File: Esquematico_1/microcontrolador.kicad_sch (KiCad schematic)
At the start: 33 parts, among them U2 STM32F405RGTx

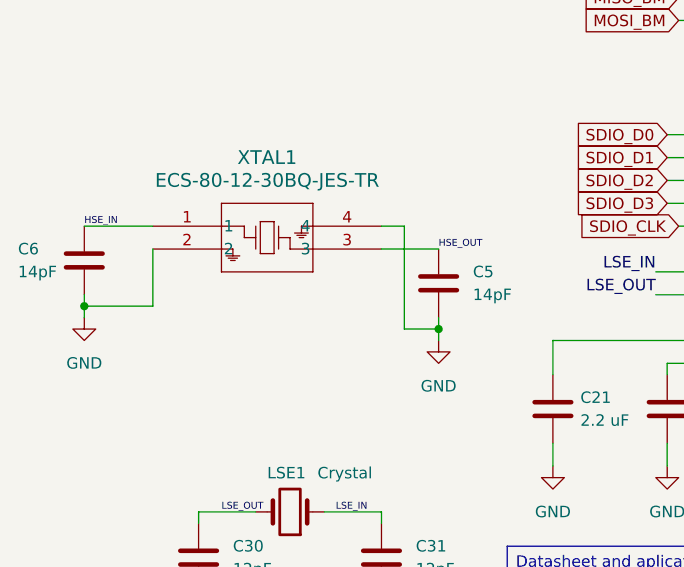
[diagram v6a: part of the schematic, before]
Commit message: asignación de footprints
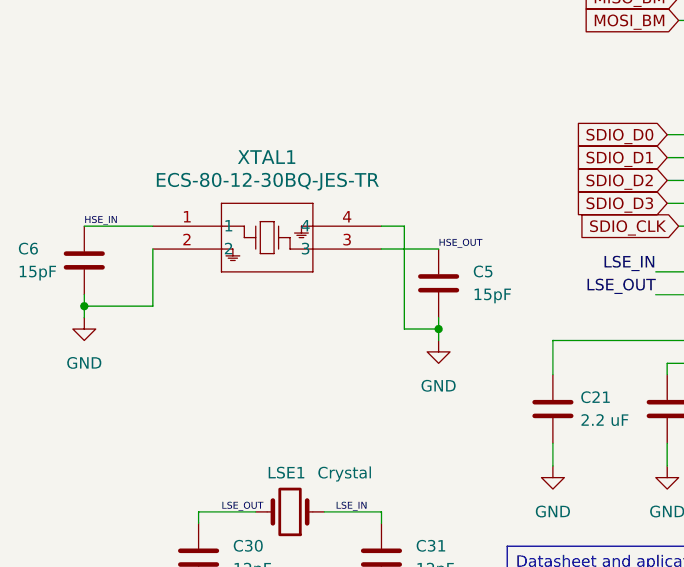
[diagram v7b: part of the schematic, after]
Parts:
- C5, C6: value 14pF -> 15pF; footprint Capacitor_SMD:C_0402_1005Metric_Pad0.74x0.62mm_HandSolder -> Capacitor_SMD:C_0201_0603Metric_Pad0.64x0.40mm_HandSolder
- XTAL1: footprint ECS-80-12_ECS -> ESCMHZ:ECS-80-12_ECS
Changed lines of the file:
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@@
 			)
 		)
-		(property "Value" "14pF"
+		(property "Value" "15pF"
 			(at 16.764 100.33 0)
 			(effects
@@
 			)
 		)
-		(property "Footprint" "Capacitor_SMD:C_0402_1005Metric_Pad0.74x0.62mm_HandSolder"
+		(property "Footprint" "Capacitor_SMD:C_0201_0603Metric_Pad0.64x0.40mm_HandSolder"
 			(at 25.0952 102.87 0)
 			(effects
@@
 			)
 		)
-		(property "Value" "14pF"
+		(property "Value" "15pF"
 			(at 67.31 102.8699 0)
 			(effects
@@
 			)
 		)
-		(property "Footprint" "Capacitor_SMD:C_0402_1005Metric_Pad0.74x0.62mm_HandSolder"
+		(property "Footprint" "Capacitor_SMD:C_0201_0603Metric_Pad0.64x0.40mm_HandSolder"
 			(at 64.4652 105.41 0)
 			(effects
@@
 			)
 		)
-		(property "Footprint" "ECS-80-12_ECS"
+		(property "Footprint" "ESCMHZ:ECS-80-12_ECS"
 			(at 31.75 95.25 0)
 			(effects

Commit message: Footprints
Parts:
- C20, C21, FB1: footprint (none) -> Capacitor_SMD:C_0805_2012Metric_Pad1.18x1.45mm_HandSolder
- C30, C31: footprint (none) -> Capacitor_SMD:C_0603_1608Metric_Pad1.08x0.95mm_HandSolder
- C5, C6: footprint Capacitor_SMD:C_0201_0603Metric_Pad0.64x0.40mm_HandSolder -> Capacitor_SMD:C_0603_1608Metric_Pad1.08x0.95mm_HandSolder
- R3: footprint (none) -> Resistor_SMD:R_0805_2012Metric_Pad1.20x1.40mm_HandSolder
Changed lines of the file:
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@@
 			)
 		)
-		(property "Footprint" ""
+		(property "Footprint" "Capacitor_SMD:C_0805_2012Metric_Pad1.18x1.45mm_HandSolder"
 			(at 89.8652 119.38 0)
 			(effects
@@
 			)
 		)
-		(property "Footprint" ""
+		(property "Footprint" "Capacitor_SMD:C_0805_2012Metric_Pad1.18x1.45mm_HandSolder"
 			(at 77.1652 119.38 0)
 			(effects
@@
 			)
 		)
-		(property "Footprint" "Capacitor_SMD:C_0201_0603Metric_Pad0.64x0.40mm_HandSolder"
+		(property "Footprint" "Capacitor_SMD:C_0603_1608Metric_Pad1.08x0.95mm_HandSolder"
 			(at 25.0952 102.87 0)
 			(effects
@@
 			)
 		)
-		(property "Footprint" ""
+		(property "Footprint" "Capacitor_SMD:C_0805_2012Metric_Pad1.18x1.45mm_HandSolder"
 			(at 40.64 57.658 90)
 			(effects
@@
 			)
 		)
-		(property "Footprint" "Capacitor_SMD:C_0201_0603Metric_Pad0.64x0.40mm_HandSolder"
+		(property "Footprint" "Capacitor_SMD:C_0603_1608Metric_Pad1.08x0.95mm_HandSolder"
 			(at 64.4652 105.41 0)
 			(effects
@@
 			)
 		)
-		(property "Footprint" ""
+		(property "Footprint" "Capacitor_SMD:C_0603_1608Metric_Pad1.08x0.95mm_HandSolder"
 			(at 37.7952 135.89 0)
 			(effects
@@
 			)
 		)
-		(property "Footprint" ""
+		(property "Footprint" "Capacitor_SMD:C_0603_1608Metric_Pad1.08x0.95mm_HandSolder"
 			(at 58.1152 135.89 0)
 			(effects
@@
 			)
 		)
-		(property "Footprint" ""
+		(property "Footprint" "Resistor_SMD:R_0805_2012Metric_Pad1.20x1.40mm_HandSolder"
 			(at 250.952 38.1 90)
 			(effects
